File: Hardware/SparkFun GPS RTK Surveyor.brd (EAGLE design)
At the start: 69.1 x 109.1 mm, 162 parts, among them J2 CONN_04, J3 USB-C, J4 Qwiic Right Angle, J6 Start Base, J7 Power Switch, J9 CONN_04, Q2 MBT3904DW1T1, U1 MCP73831, U2 3.3V, U3 ZED-F9P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

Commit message: Production of v10
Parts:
- removed D9: BLUE, SparkFun-LED:LED-0603
- removed JP9: (no value), SparkFun-Jumpers:SMT-JUMPER_3_2-NC_TRACE_SILK
- removed R13: 1k, SparkFun-Resistors:0603
- removed R18, R19, R6: 33, SparkFun-Resistors:0603
- removed R21, R22: 2.2k, SparkFun-Resistors:0603
- added C14: 10uF, SparkFun-Capacitors:0603
- added J11, J12, J13, J14: (no value), SparkFun-Connectors:1X04_NO_SILK
- added J15: (no value), SparkFun-Connectors:1X02_NO_SILK
- added U$65: (no value), output:#ESP32#RST#0
- added U$66: (no value), output:#20MM#0
- added U$67: (no value), output:#100MM#1
- added U$68: (no value), output:#1000MM#2
- J1: device SparkFun-Connectors:1X08_NO_SILK -> SparkFun-Connectors:1X04_NO_SILK
- R4: device SparkFun-Resistors:0603 -> SparkFun-Resistors:1206_RA
- S1, S4: device SparkFun-Switches:TACTILE_SWITCH_SMD_6.0X3.5MM -> SparkFun-Switches:TACTILE_SWITCH_SMD_5.2MM
- U$11: device output:#STAT#0 -> output:#PPS#0
- U$15: device output:#FEN#0 -> SparkFun GPS RTK Surveyor:LIGHT_PIPE_3MM
- U$60: device buzzard_labels (8):RST3 -> output:#ESP32#IO0#0
- moved R38 164.1 mm to (-1.27, 82.5), flipped to the bottom, turned to 180 degrees
- moved R29 161.3 mm to (5.08, 90.2), flipped to the bottom, turned to 0 degrees
- moved R23 160.3 mm to (5.08, 85.1), flipped to the bottom, turned to 180 degrees
- moved R37 159.8 mm to (-1.27, 95.2), flipped to the bottom, turned to 180 degrees
- moved F1 153.2 mm to (5.08, 80.0), flipped to the bottom, turned to 270 degrees
- moved J3 151.1 mm to (2.54, 88.9), flipped to the bottom
- moved U6 150.0 mm to (11.4, 87.6), flipped to the bottom, turned to 270 degrees
- moved D15 148.6 mm to (16.5, 80.0), flipped to the bottom
- moved BYP 148.1 mm to (1.27, 80.0), flipped to the bottom, turned to 270 degrees
- moved LED1 146.3 mm to (15.0, 80.0), flipped to the bottom
- moved R20 144.9 mm to (39.9, 97.8), flipped to the bottom
- moved Q2 143.8 mm to (5.08, 87.6), flipped to the bottom
- moved S1 141.0 mm to (55.9, 95.2), turned to 270 degrees
- moved R33 140.2 mm to (16.5, 76.2), flipped to the bottom, turned to 270 degrees
- moved C13 139.1 mm to (38.4, 97.8), flipped to the bottom, turned to 270 degrees
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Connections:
- removed net !RESET: J1.6, R2.P5
- removed net !SAFE: J1.7, R2.P6
- removed net ATMEGA328_D10: R26.1
- removed net ATMEGA328_D13_SCK: R34.1
- removed net ATMEGA328_D2: J6.1
- removed net ATMEGA328_D6: R24.1
- removed net ATMEGA328_D9: R25.1
- removed net ESP32_IO12_MISO1: U5.14
- removed net ESP32_IO13_MOSI1: U5.16
- removed net ESP32_IO15: U5.23
- removed net ESP32_IO2: U5.24
- removed net ESP32_IO4: U5.26
- removed net ESP32_IO5: R10.2, U5.29
- removed net EXTERNAL_SERIAL2_RXI: J9.3
- removed net EXTERNAL_SERIAL2_TXO: J9.2
- removed net N$14: R6.1, U3.26
- removed net N$19: R18.1, U3.20
- removed net N$20: R19.1, U3.19
- removed net N$23: D9.A, R10.1
- removed net N$7: D4.A, R13.1
- removed net SCL_PU1: JP9.1, R21.2
- removed net SDA_PU1: JP9.3, R22.2
- removed net SHLD: J3.SHLD1, J3.SHLD2, J3.SHLD3, J3.SHLD4
- removed net TX2_P: R4.1, U3.27
- new net !SAFE!: J13.2, R2.P6
- new net ESP32_12/BLUETOOTH_STATUS: R10.1, U5.14
- new net ESP32_13/POSACC1: R24.1, U5.16
- new net ESP32_15/POSACC2: R25.1, U5.23
- new net ESP32_2/POSACC3: R26.1, U5.24
- new net ESP32_4/BASE_STAT: R34.1, U5.26
- new net ESP32_5/BASE_SELECT: J6.1, U5.29
- new net FENCE_LV: R4.P8, U3.19
- new net N$3: D4.A, R10.2
- new net RTK_LV: R4.P7, U3.20
- new net RX2_LV: R4.P6, U3.26
- new net TX2_LV: R4.P5, U3.27
- new net ZED_!RESET!: J13.3, R2.P5
- net 3.3V: now also C14.1, J1.4, J12.4, R12.2; no longer J1.1, JP9.2
- net 5V: now also J11.4, J7.1; no longer J7.2
- net ESP32_EN: now also S1.3, S1.4; no longer S1.2
- net ESP32_I34: now also J14.2
- net ESP32_I35: now also J14.1
- net ESP32_IO0: now also S4.3, S4.4; no longer S4.2
- net ESP32_IO21_SDA: no longer R22.1
- net ESP32_IO22_SCL: no longer R21.1
- net ESP32_IO32: now also J14.4
- net ESP32_IO33: now also J14.3
- net EXTERNAL_SERIAL1_RXI: now also J12.2
- net EXTERNAL_SERIAL1_TXO: now also J12.3
- net FENCE_STAT: now also J1.2, R4.P1; no longer J1.5, R13.2, R19.2
- net GND: now also C14.2, J1.1, J11.1, J12.1, J3.SHLD1, J3.SHLD2, J3.SHLD3, J3.SHLD4, S1.2, S4.2; no longer D3.C, D9.C, J1.8
- net PPS_STAT: now also J13.1; no longer J1.3
- net RTK_STAT: now also D3.C, J1.3, R4.P2; no longer J1.4, R12.2, R18.2
- net TX_READY: now also J13.4; no longer J1.2
- net VBATT_SWTICHED: now also J7.2; no longer J7.1
- net ZED-RXI1: now also J15.2
- net ZED-RXI2: now also J11.2, J9.3, R4.P3; no longer R6.2
- net ZED-TXO1: now also J15.1
- net ZED-TXO2: now also J11.3, J9.2, R4.P4; no longer R4.2
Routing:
- net 3.3V: track 0.00 -> 260.5 mm, vias 0 -> 6
- net 5V: track 2.55 -> 259.5 mm, vias 0 -> 8
- net VBATT_SWTICHED: track 0.00 -> 109.5 mm, vias 0 -> 5
- net CHG_LED: track 0.00 -> 98.0 mm, vias 0 -> 4
- net ESP32_IO16_RXI2: track 0.00 -> 94.7 mm, vias 0 -> 5
- net ESP32_IO17_TXO2: track 0.00 -> 93.6 mm, vias 0 -> 5
- net ZED-TXO2: track 0.00 -> 87.3 mm, vias 0 -> 3
- net ESP32_EN: track 0.00 -> 83.4 mm, vias 0 -> 2
- net SDA: track 0.00 -> 82.0 mm, vias 0 -> 4
- net SCL: track 0.00 -> 81.6 mm, vias 0 -> 4
- net EXTERNAL_SERIAL1_RXI: track 0.00 -> 81.3 mm, vias 0 -> 2
- net ESP32_5/BASE_SELECT: track 0.00 -> 80.0 mm, vias 0 -> 3
- net ZED-RXI2: track 0.00 -> 80.0 mm, vias 0 -> 3
- net EXTERNAL_SERIAL1_TXO: track 0.00 -> 79.6 mm, vias 0 -> 3
- net ESP32_IO0: track 0.00 -> 56.9 mm, vias 0 -> 3
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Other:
- outline, holes or cut-outs redrawn

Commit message: Update SparkFun GPS RTK Surveyor.brd
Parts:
- added U$69: (no value), output:#BYP#0
- moved LOGO1 7.01 mm to (-5.08, 73.7)
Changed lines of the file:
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@@
 <text x="128.27" y="24.13" size="0.5" layer="51" font="vector" ratio="15" align="center">Recommended air gap: 0.5-1.27mm</text>
 <text x="128.27" y="20.32" size="0.5" layer="51" font="vector" ratio="15" align="center">LFB037CTP-ND</text>
-<text x="10.16" y="97.79" size="1.778" layer="21" font="vector" ratio="15" align="center">-</text>
-<text x="10.16" y="102.87" size="1.778" layer="21" font="vector" ratio="15" align="center">+</text>
+<text x="12.954" y="96.901" size="1.778" layer="21" font="vector" ratio="15" align="center">-</text>
+<text x="12.827" y="103.886" size="1.778" layer="21" font="vector" ratio="15" align="center">+</text>
 <text x="100.33" y="22.86" size="0.5" layer="51" font="vector" ratio="15" align="center">Gap to base switch: 3.4mm</text>
 <text x="114.3" y="22.86" size="0.5" layer="51" font="vector" ratio="15" align="center">Top Cover thickness: 2.25mm</text>
@@
 <attribute name="VALUE" value="Qwiic Right Angle" x="37.465" y="4.699" size="1.778" layer="27" display="off"/>
 </element>
-<element name="LOGO1" library="SparkFun-Aesthetics" package="OSHW-LOGO-MINI" value="OSHW-LOGOMINI" x="-4.45" y="80.64" smashed="yes" rot="MR0"/>
+<element name="LOGO1" library="SparkFun-Aesthetics" package="OSHW-LOGO-MINI" value="OSHW-LOGOMINI" x="-5.08" y="73.66" smashed="yes" rot="MR0"/>
 <element name="C3" library="SparkFun-Capacitors" package="0603" value="1.0uF" x="24.13" y="41.91" smashed="yes">
 <attribute name="NAME" x="24.13" y="42.672" size="0.6096" layer="25" font="vector" ratio="20" align="bottom-center"/>
@@
 <element name="U$67" library="output" package="#100MM#1" value="" x="29.464" y="50.546" smashed="yes"/>
 <element name="U$68" library="output" package="#1000MM#2" value="" x="29.083" y="42.926" smashed="yes"/>
+<element name="U$69" library="output" package="#BYP#0" value="" x="0.635" y="80.01" smashed="yes" rot="MR0"/>
 </elements>
 <signals>
@@
 <contactref element="J1" pad="4"/>
 <wire x1="46.482" y1="30.48" x2="45.72" y2="30.48" width="0.5588" layer="1"/>
-<wire x1="47.655" y1="29.307" x2="47.3075" y2="29.6545" width="0.5588" layer="1"/>
-<wire x1="47.3075" y1="29.6545" x2="46.482" y2="30.48" width="0.5588" layer="1"/>
+<wire x1="47.7139" y1="29.2481" x2="46.482" y2="30.48" width="0.5588" layer="1"/>
 <wire x1="37.846" y1="12.065" x2="45.72" y2="12.065" width="0.5588" layer="1"/>
 <wire x1="29.09" y1="41.91" x2="29.09" y2="45.586" width="0.5588" layer="1"/>
@@
 <wire x1="45.72" y1="5.334" x2="45.72" y2="6.985" width="0.5588" layer="1"/>
 <wire x1="45.72" y1="6.985" x2="45.72" y2="12.065" width="0.5588" layer="1"/>
-<wire x1="45.72" y1="12.065" x2="45.72" y2="17.399" width="0.5588" layer="1"/>
-<wire x1="45.72" y1="17.399" x2="47.7139" y2="19.3929" width="0.5588" layer="1"/>
-<wire x1="47.7139" y1="29.2481" x2="47.655" y2="29.307" width="0.5588" layer="1"/>
-<wire x1="47.7139" y1="19.3929" x2="47.7139" y2="29.2481" width="0.5588" layer="1"/>
+<wire x1="45.72" y1="12.065" x2="47.7139" y2="14.0589" width="0.5588" layer="1"/>
+<wire x1="47.7139" y1="14.0589" x2="47.7139" y2="29.2481" width="0.5588" layer="1"/>
 </signal>
 <signal name="GND">

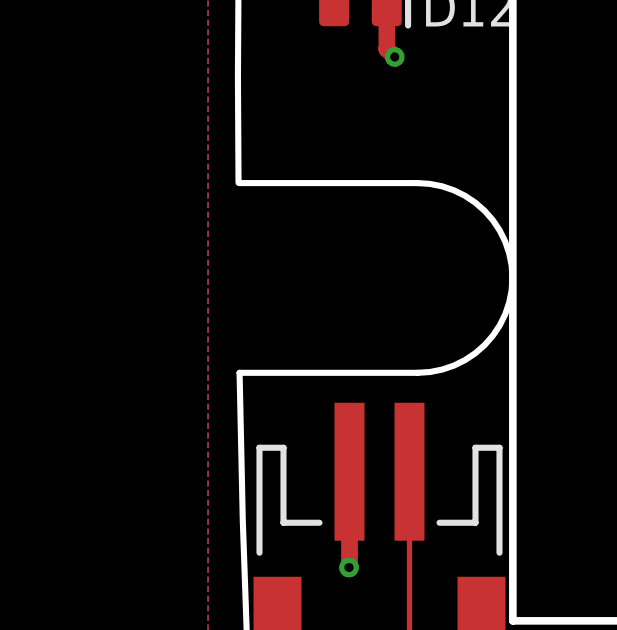
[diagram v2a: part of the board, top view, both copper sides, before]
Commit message: Completed 4 layer design with 4pin SMD JST connectors
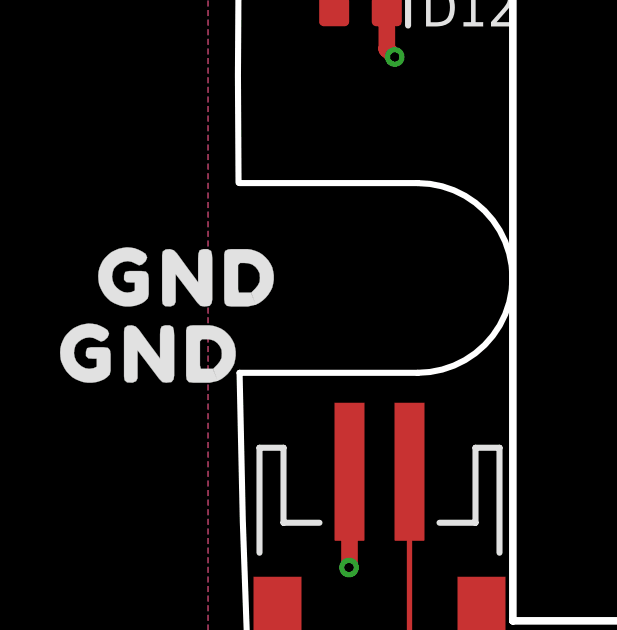
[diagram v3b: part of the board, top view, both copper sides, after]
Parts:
- added U$70, U$71: (no value), output:GND0
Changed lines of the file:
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@@
 <?xml version="1.0" encoding="utf-8"?>
 <!DOCTYPE eagle SYSTEM "eagle.dtd">
-<eagle version="9.5.2">
+<eagle version="9.6.0">
 <drawing>
 <settings>
@@
 <grid distance="0.05" unitdist="inch" unit="inch" style="lines" multiple="1" display="yes" altdistance="0.005" altunitdist="inch" altunit="inch"/>
 <layers>
-<layer number="1" name="Top" color="4" fill="1" visible="yes" active="yes"/>
+<layer number="1" name="Top" color="4" fill="1" visible="no" active="yes"/>
 <layer number="2" name="Horz/GND" color="1" fill="3" visible="no" active="yes"/>
 <layer number="15" name="Vert" color="4" fill="6" visible="no" active="yes"/>
-<layer number="16" name="Bottom" color="1" fill="1" visible="yes" active="yes"/>
+<layer number="16" name="Bottom" color="1" fill="1" visible="no" active="yes"/>
 <layer number="17" name="Pads" color="2" fill="1" visible="yes" active="yes"/>
-<layer number="18" name="Vias" color="2" fill="1" visible="yes" active="yes"/>
-<layer number="19" name="Unrouted" color="6" fill="1" visible="yes" active="yes"/>
+<layer number="18" name="Vias" color="2" fill="1" visible="no" active="yes"/>
+<layer number="19" name="Unrouted" color="6" fill="1" visible="no" active="yes"/>
 <layer number="20" name="Dimension" color="24" fill="1" visible="yes" active="yes"/>
 <layer number="21" name="tPlace" color="16" fill="1" visible="yes" active="yes"/>
-<layer number="22" name="bPlace" color="14" fill="1" visible="yes" active="yes"/>
+<layer number="22" name="bPlace" color="14" fill="1" visible="no" active="yes"/>
 <layer number="23" name="tOrigins" color="15" fill="1" visible="yes" active="yes"/>
-<layer number="24" name="bOrigins" color="15" fill="1" visible="yes" active="yes"/>
+<layer number="24" name="bOrigins" color="15" fill="1" visible="no" active="yes"/>
 <layer number="25" name="tNames" color="7" fill="1" visible="no" active="yes"/>
 <layer number="26" name="bNames" color="7" fill="1" visible="no" active="yes"/>
-<layer number="27" name="tValues" color="7" fill="1" visible="no" active="yes"/>
+<layer number="27" name="tValues" color="7" fill="1" visible="yes" active="yes"/>
 <layer number="28" name="bValues" color="7" fill="1" visible="no" active="yes"/>
 <layer number="29" name="tStop" color="7" fill="3" visible="no" active="yes"/>
 <layer number="30" name="bStop" color="7" fill="6" visible="no" active="yes"/>
-<layer number="31" name="tCream" color="7" fill="4" visible="no" active="yes"/>
+<layer number="31" name="tCream" color="7" fill="4" visible="yes" active="yes"/>
 <layer number="32" name="bCream" color="7" fill="5" visible="no" active="yes"/>
 <layer number="33" name="tFinish" color="6" fill="3" visible="no" active="yes"/>
@@
 <layer number="47" name="Measures" color="7" fill="1" visible="no" active="yes"/>
 <layer number="48" name="Document" color="7" fill="1" visible="no" active="yes"/>
-<layer number="49" name="Reference" color="7" fill="1" visible="yes" active="yes"/>
+<layer number="49" name="Reference" color="7" fill="1" visible="no" active="yes"/>
 <layer number="50" name="dxf" color="7" fill="1" visible="no" active="yes"/>
 <layer number="51" name="tDocu" color="6" fill="1" visible="yes" active="yes"/>
@@
 <element name="U$68" library="output" package="#1000MM#2" value="" x="29.083" y="42.926" smashed="yes"/>
 <element name="U$69" library="output" package="#BYP#0" value="" x="0.635" y="80.01" smashed="yes" rot="MR0"/>
+<element name="U$70" library="output" package="GND0" value="" x="-13.97" y="52.07" smashed="yes"/>
+<element name="U$71" library="output" package="GND0" value="" x="-15.24" y="49.53" smashed="yes"/>
 </elements>
 <signals>
